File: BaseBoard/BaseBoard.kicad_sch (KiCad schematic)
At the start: 9 parts, among them J2 54-00167, J3 SSD1306 OLED Display, J4 FAN, U10 USB Type C, U11 PRTR5V0U2X

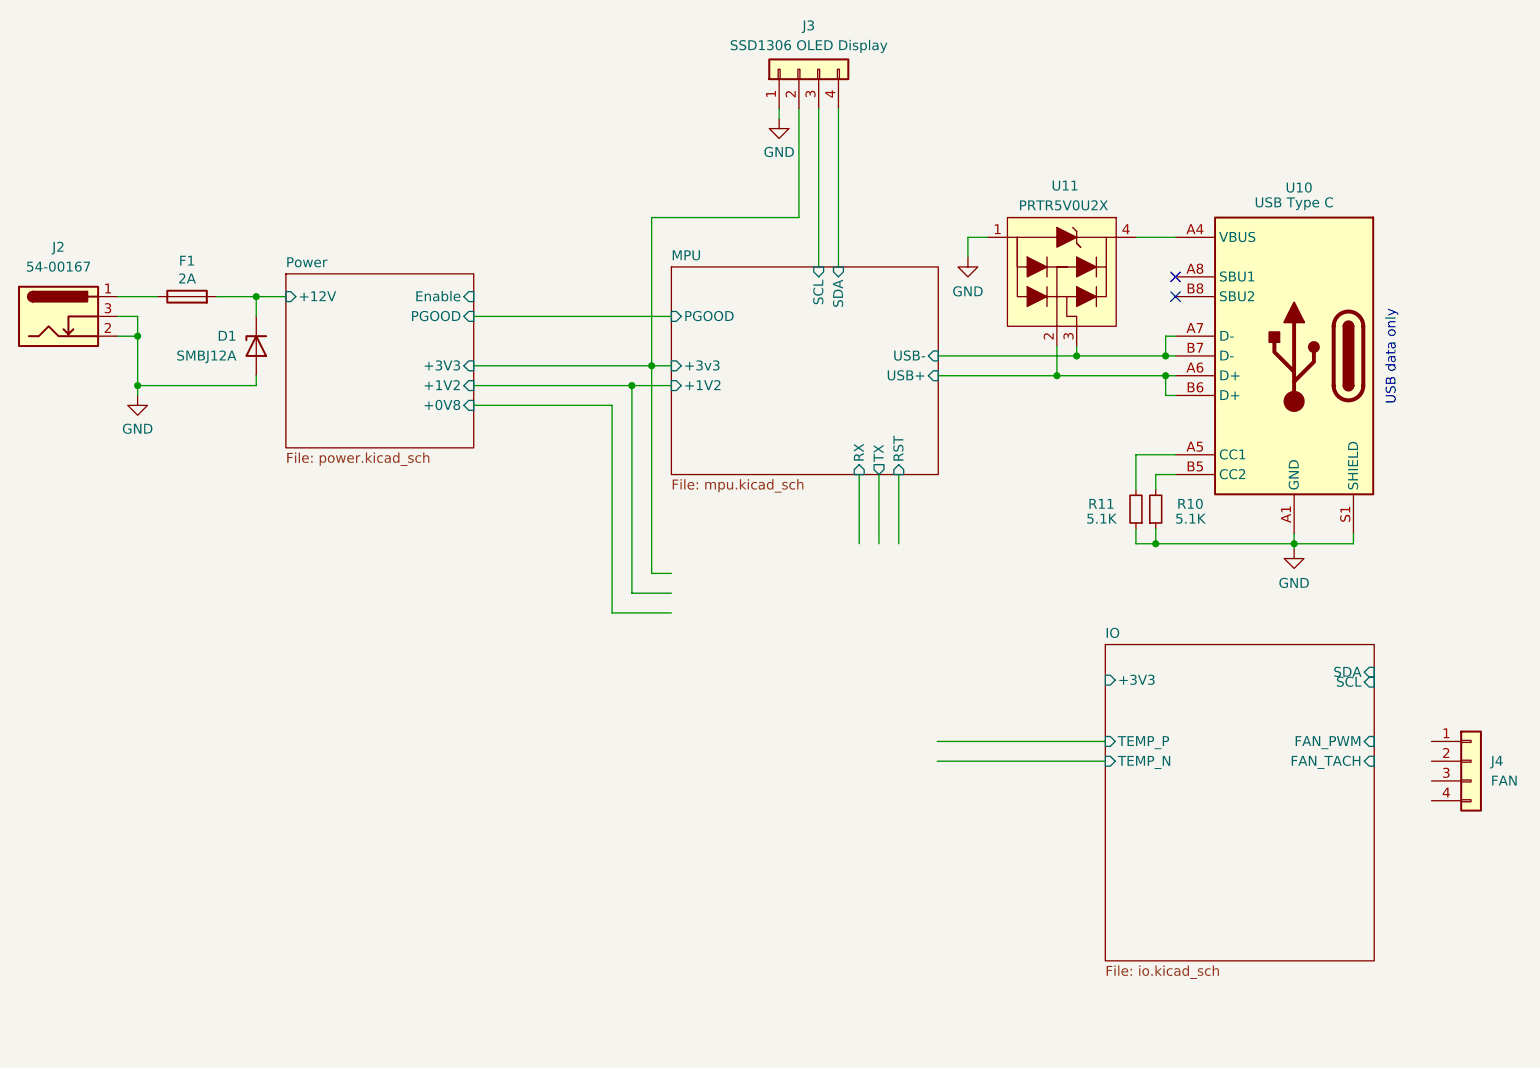
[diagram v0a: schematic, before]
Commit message: Added support for TMP1075 temperature sensor to monitor ASIC
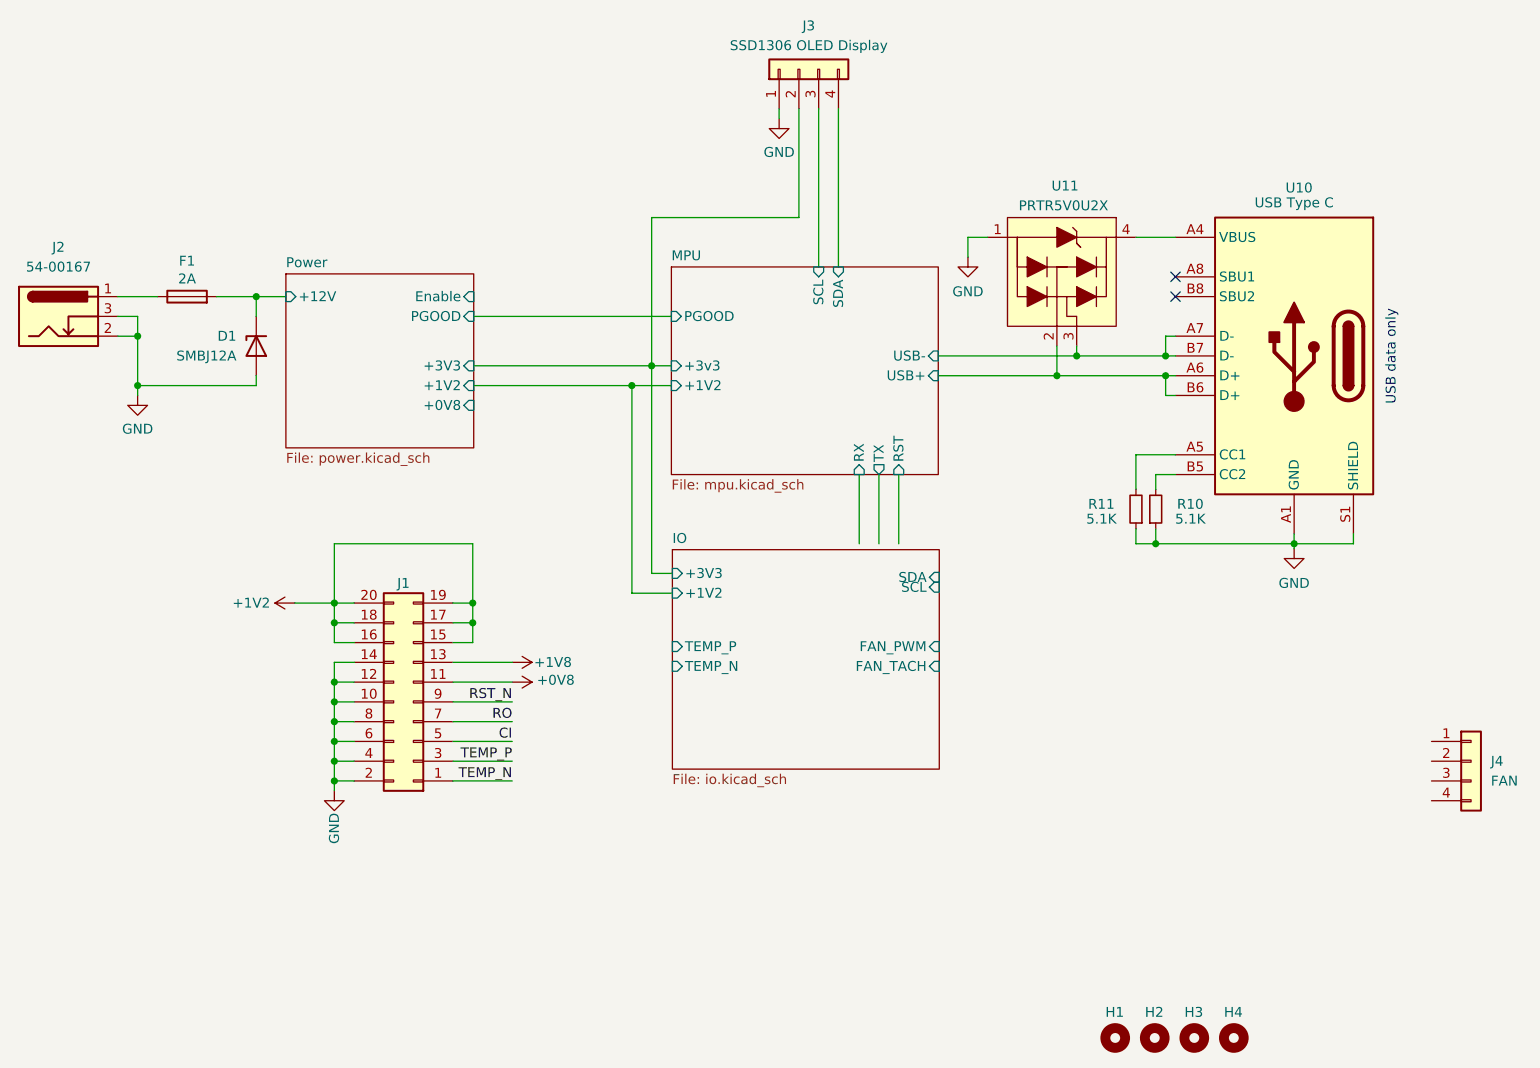
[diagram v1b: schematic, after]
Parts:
- added H1, H2, H3, H4: MountingHole, MountingHole:MountingHole_3.2mm_M3, symbol Mechanical:MountingHole
- added J1: Conn_02x10_Odd_Even, Connector_PinHeader_2.54mm:PinHeader_2x10_P2.54mm_Vertical, symbol Connector_Generic:Conn_02x10_Odd_Even
- J3, J4: footprint (none) -> Connector_JST:JST_PH_B4B-PH-K_1x04_P2.00mm_Vertical
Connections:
- net GND: now also J1.10 (Pin_10), J1.12 (Pin_12), J1.14 (Pin_14), J1.2 (Pin_2), J1.4 (Pin_4), J1.6 (Pin_6), J1.8 (Pin_8)
- new net +0V8: J1.11 (Pin_11)
- new net +1V2: J1.15 (Pin_15), J1.16 (Pin_16), J1.17 (Pin_17), J1.18 (Pin_18), J1.19 (Pin_19), J1.20 (Pin_20)
- new net +1V8: J1.13 (Pin_13)
- new net CI: J1.5 (Pin_5)
- new net RO: J1.7 (Pin_7)
- new net RST_N: J1.9 (Pin_9)
- new net TEMP_N: J1.1 (Pin_1)
- new net TEMP_P: J1.3 (Pin_3)
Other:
- sheet IO ports: added +1V2; removed none
